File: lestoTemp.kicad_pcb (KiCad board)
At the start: 2 copper layers, 20 x 19.8 mm, 22 parts, among them J1 PRG, J2 PWR, J3 RST, J4 PRG, J5 SLP, Q1 Q_NPN_BCE, U1 ESP-12E, U2 DHT11, U3 BME280

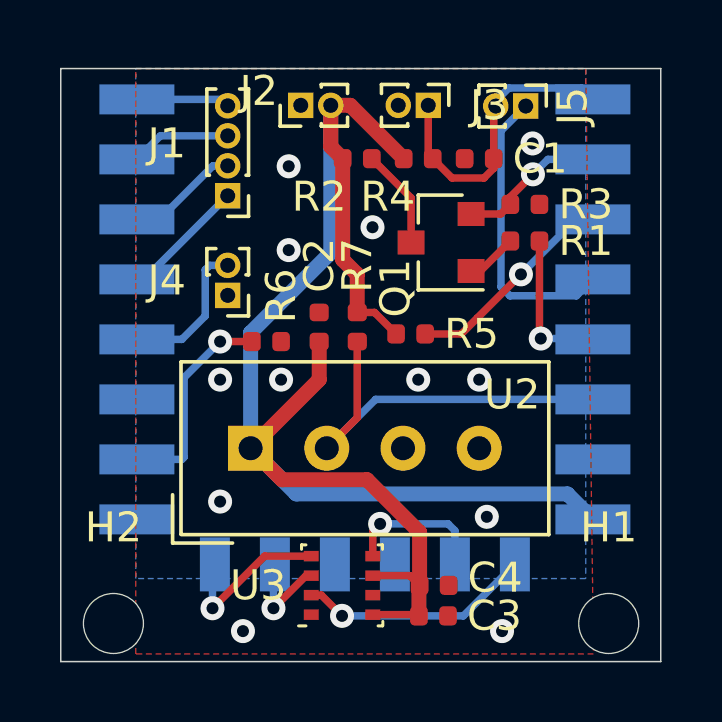
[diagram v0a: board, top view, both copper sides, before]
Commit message: fixed spi for V2, numerous pin changess
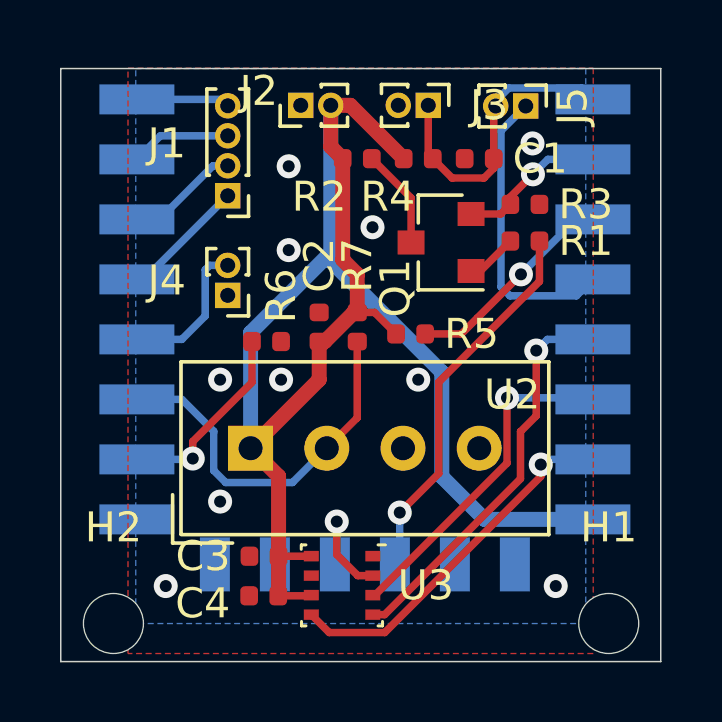
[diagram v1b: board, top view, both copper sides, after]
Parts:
- moved C3 5.99 mm to (84.8, 108.8), turned to 180 degrees
- moved C4 5.69 mm to (84.8, 110.1), turned to 180 degrees
- turned U3 to 270 degrees
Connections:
- R7 pad 2: GPIO12 -> GPIO2
- U1 pad 10: SDI -> Net-(U1-Pad10)
- U1 pad 11: Net-(U1-Pad11) -> GPIO14
- U1 pad 12: Net-(U1-Pad12) -> CS
- U1 pad 13: SDO -> Net-(U1-Pad13)
- U1 pad 14: CLK -> Net-(U1-Pad14)
- U1 pad 17: Net-(U1-Pad17) -> GPIO2
- U1 pad 5: GPIO14 -> CLK
- U1 pad 6: GPIO12 -> SDO
- U1 pad 7: Net-(U1-Pad7) -> SDI
- U1 pad 9: CS -> Net-(U1-Pad9)
- U2 pad 2: GPIO12 -> GPIO2
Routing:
- net GPIO12: track 13.5 -> 0.00 mm
- net GPIO2: track 0.00 -> 12.7 mm
- net SDO: track 3.19 -> 11.4 mm
- net CLK: track 5.51 -> 13.3 mm
- net GPIO14: track 5.02 -> 12.8 mm
- net SDI: track 4.89 -> 12.3 mm
- net CS: track 7.78 -> 4.05 mm
- net +3V3: track 54.3 -> 52.9 mm
- net GND: vias 12 -> 10
